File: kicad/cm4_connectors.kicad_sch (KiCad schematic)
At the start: 4 parts, among them U12 2541WV-2X12P

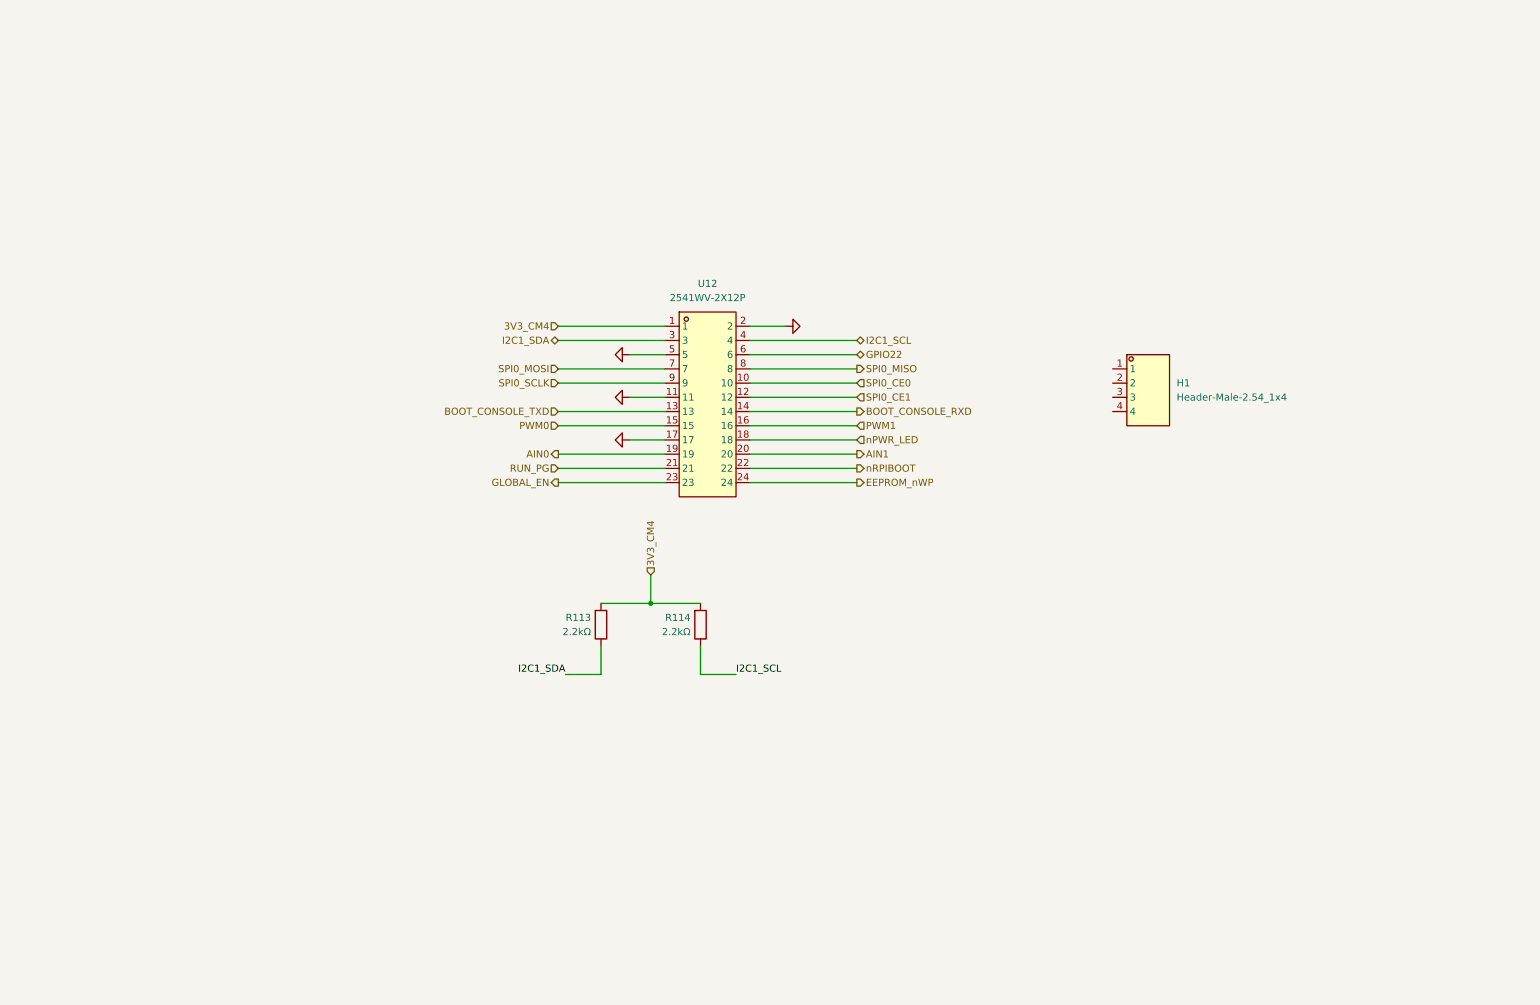
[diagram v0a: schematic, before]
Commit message: GPIO connectors defined
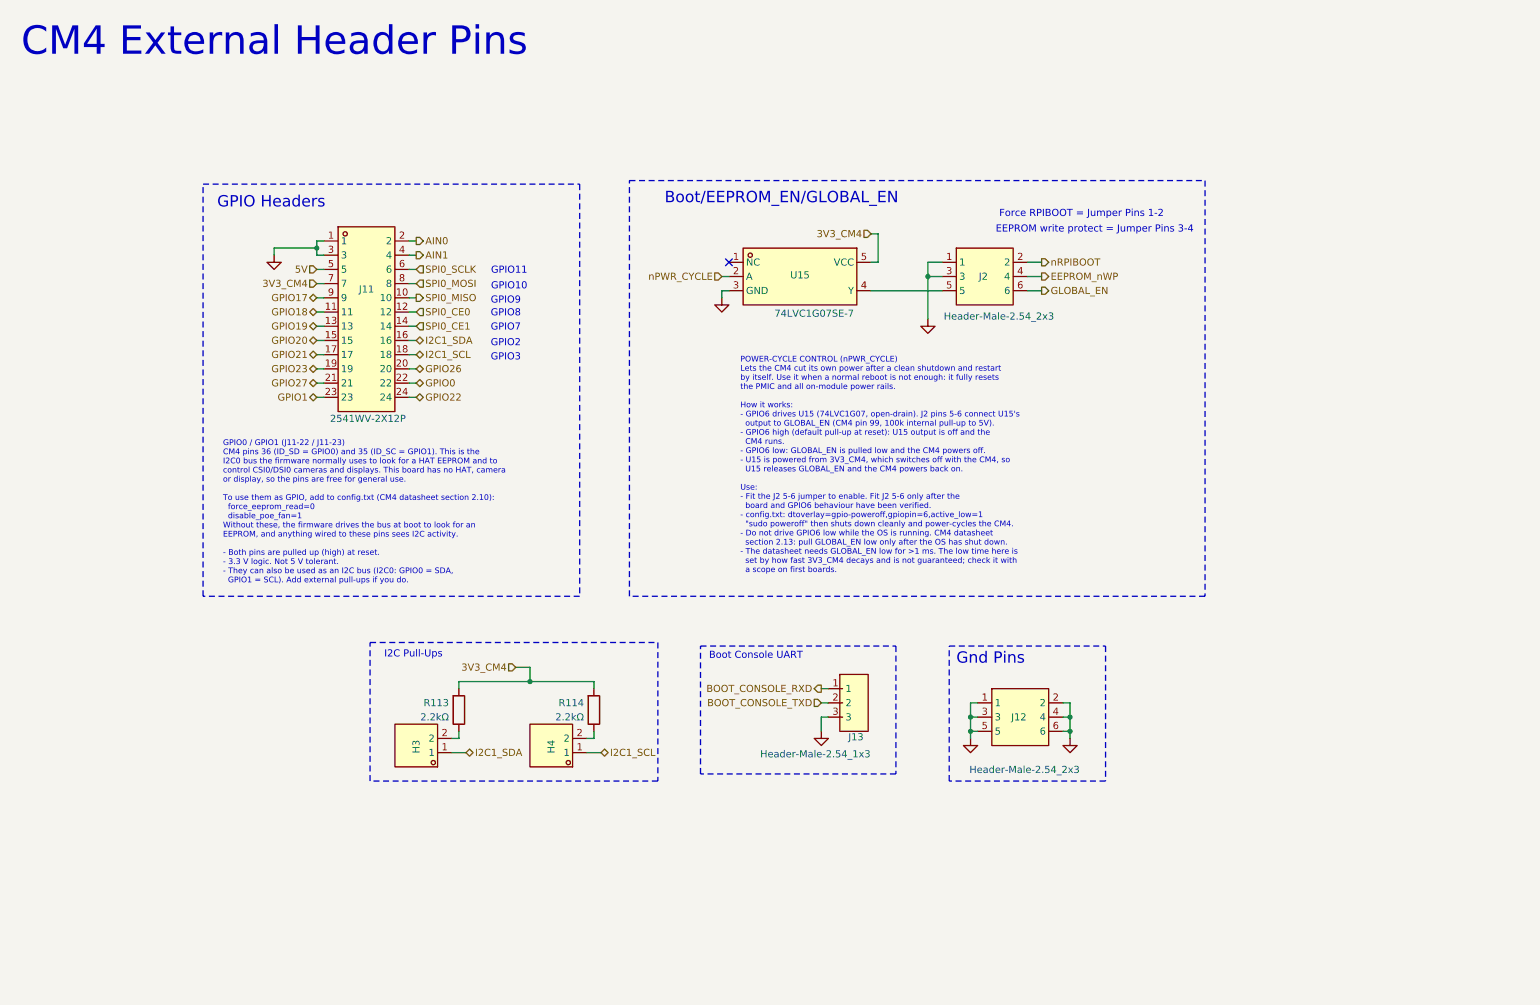
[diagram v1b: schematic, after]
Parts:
- removed H1: Header-Male-2.54_1x4, MyParts:HDR-TH_4P-P2.54-V-M, symbol MyParts:Header-Male-2.54_1x4
- removed U12: 2541WV-2X12P, MyParts:HDR-TH_24P-P2.54-V-M-R2-C12-S2.54, symbol MyParts:2541WV-2X12P
- added H3, H4: 210S-1*2P L=11.6MMGold-plated black, MyParts:HDR-TH_2P-P2.54-V-M-1, symbol MyParts:210S-1*2PL=11.6MMGold-platedblack
- added J11: 2541WV-2X12P, MyParts:HDR-TH_24P-P2.54-V-M-R2-C12-S2.54, symbol MyParts:2541WV-2X12P
- added J12, J2: Header-Male-2.54_2x3, MyParts:HDR-TH_6P-P2.54-V-M-R2-C3-S2.54-1, symbol MyParts:Header-Male-2.54_2x3
- added J13: Header-Male-2.54_1x3, MyParts:HDR-TH_3P-P2.54-V-M-1, symbol MyParts:Header-Male-2.54_1x3
- added U15: 74LVC1G07SE-7, MyParts:SC-88A_L2.0-W1.3-P0.65-LS2.1-BL, symbol MyParts:74LVC1G07SE-7
- R113, R114: footprint PCM_JLCPCB:R_0402 -> MyParts:R0402; symbol PCM_JLCPCB-Resistors:0402,2.2kΩ -> MyParts:0402WGF2201TCE; Attrition Qty 10 -> (none); Category Resistors,Chip Resistor - Surface Mount -> (none); Class Basic Component -> (none); LCSC C25879 -> (none); LCSC Part (none) -> C25879; MPN (none) -> 0402WGF2201TCE; Manufacturer UNI-ROYAL(Uniroyal Elec) -> UNI-ROYAL; Minimum Qty 20 -> (none); Operating Temperature Range -55°C~+155°C -> (none); Overload Voltage (Max) 50V -> (none); Part 0402WGF2201TCE -> (none); Power(Watts) 62.5mW -> (none); Price 0.004USD -> (none); Process SMT -> (none); Resistance 2.2kΩ -> (none); Stock 1767502 -> (none); Temperature Coefficient ±100ppm/°C -> (none); Type Thick Film Resistors -> (none); Voltage Rating (none) -> 50V
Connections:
- net 3V3_CM4: now also J11.7, U15.5 (VCC)
- net AIN0: now also J11.2
- net AIN1: now also J11.4
- net BOOT_CONSOLE_RXD: now also J13.1
- net BOOT_CONSOLE_TXD: now also J13.2
- net EEPROM_nWP: now also J2.4
- net GLOBAL_EN: now also J2.6
- net GND: now also J11.1, J11.3, J12.1, J12.2, J12.3, J12.4, J12.5, J12.6, J13.3, J2.1, J2.3, U15.3 (GND)
- net GPIO22: now also J11.24
- net I2C1_SCL: now also H4.1, J11.18; no longer R114.2
- net I2C1_SDA: now also H3.1, J11.16; no longer R113.2
- net SPI0_CE0: now also J11.12
- net SPI0_CE1: now also J11.14
- net SPI0_MISO: now also J11.10
- net SPI0_MOSI: now also J11.8
- net SPI0_SCLK: now also J11.6
- net nRPIBOOT: now also J2.2
- new net: H3.2, R113.2
- new net: J2.5, U15.4 (Y)
- new net: H4.2, R114.2
- new net 5V: J11.5
- new net GPIO0: J11.22
- new net GPIO1: J11.23
- new net GPIO17: J11.9
- new net GPIO18: J11.11
- new net GPIO19: J11.13
- new net GPIO20: J11.15
- new net GPIO21: J11.17
- new net GPIO23: J11.19
- new net GPIO26: J11.20
- new net GPIO27: J11.21
- new net nPWR_CYCLE: U15.2 (A)
- no-connect marks 0 -> 1
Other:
- note added: "Boot Console UART"
- note added: "Boot/EEPROM_EN/GLOBAL_EN"
- note added: "CM4 External Header Pins"
- note added: "EEPROM write protect = Jumper Pins 3-4"
- note added: "Force RPIBOOT = Jumper Pins 1-2"
- note added: "GPIO Headers"
- note added: "GPIO0 / GPIO1 (J11-22 / J11-23) CM4 pins 36 (ID_SD = GPIO0) and 35 (ID_SC = GPIO1). This is the I2C0 bus the firmware normally uses to look for a HAT EEPROM and to control CSI0/DSI0 cameras and displays. This board has no HAT, camera or display, so the pins are free for general use. To use them as GPIO, add to config.txt (CM4 datasheet section 2.10): force_eeprom_read=0 disable_poe_fan=1 Without 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"
- note added: "GPIO10"
- note added: "GPIO11"
- note added: "GPIO2"
- note added: "GPIO3"
- note added: "GPIO7"
- note added: "GPIO8"
- note added: "GPIO9"
- note added: "Gnd Pins"
- note added: "I2C Pull-Ups"
- note added: "POWER-CYCLE CONTROL (nPWR_CYCLE) Lets the CM4 cut its own power after a clean shutdown and restart by itself. Use it when a normal reboot is not enough: it fully resets the PMIC and all on-module power rails. How it works: - GPIO6 drives U15 (74LVC1G07, open-drain). J2 pins 5-6 connect U15's output to GLOBAL_EN (CM4 pin 99, 100k internal pull-up to 5V). - GPIO6 high (default pull-up at reset): U1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"
- moved on the sheet: R113, R114

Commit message: schematic cleanup
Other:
- note added: "H3, H4: Pull-up resistors for I2C1_SDA/I2C1_SCL. Place jumpers to apply pull-ups."
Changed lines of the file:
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@@
 	(rectangle
 		(start 80.645 130.175)
-		(end 132.08 154.94)
+		(end 132.08 163.83)
 		(stroke
 			(width 0)
@@
 		)
 	)
+	(text "H3, H4:\nPull-up resistors for I2C1_SDA/I2C1_SCL.\nPlace jumpers to apply pull-ups."
+		(exclude_from_sim no)
+		(at 87.376 158.242 0)
+		(effects
+			(font
+				(size 1.27 1.27)
+			)
+			(justify left)
+		)
+	)

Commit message: Still refining
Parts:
- H3, H4: Pkg Type (none) -> THT Pin header 1x2 P2.54
- J11: Pkg Type (none) -> THT Pin header 2x12 P2.54
- J12, J2: Pkg Type (none) -> THT Pin header 2x3 P2.54
- J13: Pkg Type (none) -> THT Pin header 1x3 P2.54
- R113, R114: Pkg Type (none) -> SMD 0402
- U15: Pkg Type (none) -> SMD SOT-353 (SC-88A)
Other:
- note added: "AIN0 / AIN1 (J11-2 / J11-4) to CM4 AnalogIP0/1 (MxL7704 ADC). Measures 0 to 2.55 V (8-bit). Input current < 1 uA (10 Mohm). Survives +6.0 V / -0.3 V DC at the connector (MxL7704 abs max). Not reverse-polarity tolerant. R133/R134 1k series (RCM4 sheet)."
- moved on the sheet: H3, H4, R113, R114

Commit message: Mods
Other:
- note added: "AIN0 / AIN1 (J11-2 / J11-4), field wired, to CM4 AnalogIP0/1 (MxL7704 ADC). Measures 0 to 2.55 V (8-bit). Survives +/-24 V either polarity: R133/R134 10k series + D54/D55 BAT54S clamps to GND and 3V3_CM4 (RCM4 sheet) hold the pins within -0.3 V / +3.6 V (abs max -0.3/+6.0). Error: ADC input < 1 uA x 10k = 10 mV, plus clamp leakage (up to ~1-2 % hot). With the CM4 off, a driven input feeds < 0.3 m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"
- note added: "EEPROM WRITE PROTECT (EEPROM_nWP, J2 3-4) The CM4 pulls EEPROM_nWP up internally (100k), so the bootloader EEPROM is writable unless J2 3-4 is fitted. The jumper only takes effect once protection is enabled in the bootloader config (CM4 datasheet 2.18). Production: - Set eeprom_write_protect=1 in the bootloader config (via usbboot or rpi-eeprom-config) before shipping. - Fit the J2 3-4 jumper. Th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"
- note added: "H3/H4: optional I2C1 pull-ups, normally OPEN. CM4 already pulls GPIO2/3 up with 1.8k (DS p.7). Fit both only for a long, high-capacitance bus at 400 kHz: ~1k total, ~2.9 mA sink at 0.4 V (I2C spec min 3 mA, so compliant devices are OK)."
- note removed: "AIN0 / AIN1 (J11-2 / J11-4) to CM4 AnalogIP0/1 (MxL7704 ADC). Measures 0 to 2.55 V (8-bit). Input current < 1 uA (10 Mohm). Survives +6.0 V / -0.3 V DC at the connector (MxL7704 abs max). Not reverse-polarity tolerant. R133/R134 1k series (RCM4 sheet)."
- note removed: "H3, H4: Pull-up resistors for I2C1_SDA/I2C1_SCL. Place jumpers to apply pull-ups."
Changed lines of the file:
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@@
 	(rectangle
 		(start 127 47.625)
-		(end 229.87 121.92)
+		(end 283.21 121.92)
 		(stroke
 			(width 0)
@@
 		)
 	)
-	(text "H3, H4:\nPull-up resistors for I2C1_SDA/I2C1_SCL.\nPlace jumpers to apply pull-ups."
+	(text "EEPROM WRITE PROTECT (EEPROM_nWP, J2 3-4)\nThe CM4 pulls EEPROM_nWP up internally (100k), so the\nbootloader EEPROM is writable unless J2 3-4 is fitted.\nThe jumper only takes effect once protection is enabled\nin the bootloader config (CM4 datasheet 2.18).\n\nProduction:\n- Set eeprom_write_protect=1 in the bootloader config\n  (via usbboot or rpi-eeprom-config) before shipping.\n- Fit the J2 3-4 jumper. The EEPROM is then protected\n  from power-up (CM4 datasheet 5.1).\n\nBootloader update:\n- Remove J2 3-4, update via usbboot or self-update,\n  then refit the jumper.\n\nWhy not a GPIO with a pull-down: CM4 EEPROM updates run\nonly via usbboot or bootloader self-update (datasheet\n6.3), before Linux can drive a GPIO, so the pin could\nnever be released for an update."
 		(exclude_from_sim no)
-		(at 125.476 187.452 0)
+		(at 231.14 84.455 0)
 		(effects
 			(font
-				(size 1.27 1.27)
+				(size 1.016 1.016)
+			)
+			(justify left)
+		)
+	)
+	(text "H3/H4: optional I2C1 pull-ups, normally OPEN.\nCM4 already pulls GPIO2/3 up with 1.8k (DS p.7).\nFit both only for a long, high-capacitance bus\nat 400 kHz: ~1k total, ~2.9 mA sink at 0.4 V\n(I2C spec min 3 mA, so compliant devices are OK)."
+		(exclude_from_sim no)
+		(at 120.65 187.452 0)
+		(effects
+			(font
+				(size 1.016 1.016)
 			)
 			(justify left)
@@
 		)
 	)
-	(text "AIN0 / AIN1 (J11-2 / J11-4)\nto CM4 AnalogIP0/1 (MxL7704 ADC).\nMeasures 0 to 2.55 V (8-bit).\nInput current < 1 uA (10 Mohm).\nSurvives +6.0 V / -0.3 V DC at\nthe connector (MxL7704 abs max).\nNot reverse-polarity tolerant.\nR133/R134 1k series (RCM4 sheet)."
+	(text "AIN0 / AIN1 (J11-2 / J11-4), field wired, to CM4\nAnalogIP0/1 (MxL7704 ADC). Measures 0 to 2.55 V (8-bit).\nSurvives +/-24 V either polarity: R133/R134 10k series\n+ D54/D55 BAT54S clamps to GND and 3V3_CM4 (RCM4 sheet)\nhold the pins within -0.3 V / +3.6 V (abs max -0.3/+6.0).\nError: ADC input < 1 uA x 10k = 10 mV, plus clamp leakage\n(up to ~1-2 % hot). With the CM4 off, a driven input feeds\n< 0.3 mA (at 6 V) into 3V3_CM4 through the upper clamp."
 		(exclude_from_sim no)
 		(at 55.626 138.176 0)
 		(effects
 			(font
-				(size 1.27 1.27)
+				(size 1.016 1.016)
 			)
 			(justify left bottom)

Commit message: Ready to start layout
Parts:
- renumbered H3 to H5, H4 to H6, J2 to J3, J11 to J4, J13 to J5, J12 to J6, R113 to R20, R114 to R21, U15 to U10
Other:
- note added: "AIN0 / AIN1 (J4-2 / J4-4), field wired, to CM4 AnalogIP0/1 (MxL7704 ADC). Measures 0 to 2.55 V (8-bit). Survives +/-24 V either polarity: R7/R6 10k series + D4/D5 BAT54S clamps to GND and 3V3_CM4 (RCM4 sheet) hold the pins within -0.3 V / +3.6 V (abs max -0.3/+6.0). Error: ADC input < 1 uA x 10k = 10 mV, plus clamp leakage (up to ~1-2 % hot). With the CM4 off, a driven input feeds < 0.3 mA (at 6 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"
- note added: "EEPROM WRITE PROTECT (EEPROM_nWP, J3 3-4) The CM4 pulls EEPROM_nWP up internally (100k), so the bootloader EEPROM is writable unless J3 3-4 is fitted. The jumper only takes effect once protection is enabled in the bootloader config (CM4 datasheet 2.18). Production: - Set eeprom_write_protect=1 in the bootloader config (via usbboot or rpi-eeprom-config) before shipping. - Fit the J3 3-4 jumper. Th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"
- note added: "GPIO0 / GPIO1 (J4-22 / J4-23) CM4 pins 36 (ID_SD = GPIO0) and 35 (ID_SC = GPIO1). This is the I2C0 bus the firmware normally uses to look for a HAT EEPROM and to control CSI0/DSI0 cameras and displays. This board has no HAT, camera or display, so the pins are free for general use. To use them as GPIO, add to config.txt (CM4 datasheet section 2.10): force_eeprom_read=0 disable_poe_fan=1 Without th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"
- note added: "H5/H6: optional I2C1 pull-ups, normally OPEN. CM4 already pulls GPIO2/3 up with 1.8k (DS p.7). Fit both only for a long, high-capacitance bus at 400 kHz: ~1k total, ~2.9 mA sink at 0.4 V (I2C spec min 3 mA, so compliant devices are OK)."
- note added: "POWER-CYCLE CONTROL (nPWR_CYCLE) Lets the CM4 cut its own power after a clean shutdown and restart by itself. Use it when a normal reboot is not enough: it fully resets the PMIC and all on-module power rails. How it works: - GPIO6 drives U10 (74LVC1G07, open-drain). J3 pins 5-6 connect U10's output to GLOBAL_EN (CM4 pin 99, 100k internal pull-up to 5V). - GPIO6 high (default pull-up at reset): U1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"
- note removed: "AIN0 / AIN1 (J11-2 / J11-4), field wired, to CM4 AnalogIP0/1 (MxL7704 ADC). Measures 0 to 2.55 V (8-bit). Survives +/-24 V either polarity: R133/R134 10k series + D54/D55 BAT54S clamps to GND and 3V3_CM4 (RCM4 sheet) hold the pins within -0.3 V / +3.6 V (abs max -0.3/+6.0). Error: ADC input < 1 uA x 10k = 10 mV, plus clamp leakage (up to ~1-2 % hot). With the CM4 off, a driven input feeds < 0.3 m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"
- note removed: "EEPROM WRITE PROTECT (EEPROM_nWP, J2 3-4) The CM4 pulls EEPROM_nWP up internally (100k), so the bootloader EEPROM is writable unless J2 3-4 is fitted. The jumper only takes effect once protection is enabled in the bootloader config (CM4 datasheet 2.18). Production: - Set eeprom_write_protect=1 in the bootloader config (via usbboot or rpi-eeprom-config) before shipping. - Fit the J2 3-4 jumper. Th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"
- note removed: "GPIO0 / GPIO1 (J11-22 / J11-23) CM4 pins 36 (ID_SD = GPIO0) and 35 (ID_SC = GPIO1). This is the I2C0 bus the firmware normally uses to look for a HAT EEPROM and to control CSI0/DSI0 cameras and displays. This board has no HAT, camera or display, so the pins are free for general use. To use them as GPIO, add to config.txt (CM4 datasheet section 2.10): force_eeprom_read=0 disable_poe_fan=1 Without 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"
- note removed: "H3/H4: optional I2C1 pull-ups, normally OPEN. CM4 already pulls GPIO2/3 up with 1.8k (DS p.7). Fit both only for a long, high-capacitance bus at 400 kHz: ~1k total, ~2.9 mA sink at 0.4 V (I2C spec min 3 mA, so compliant devices are OK)."
- note removed: "POWER-CYCLE CONTROL (nPWR_CYCLE) Lets the CM4 cut its own power after a clean shutdown and restart by itself. Use it when a normal reboot is not enough: it fully resets the PMIC and all on-module power rails. How it works: - GPIO6 drives U15 (74LVC1G07, open-drain). J2 pins 5-6 connect U15's output to GLOBAL_EN (CM4 pin 99, 100k internal pull-up to 5V). - GPIO6 high (default pull-up at reset): U1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"

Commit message: Improved README
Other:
- note added: "BOOT CONSOLE UART (J5): CM4 UART0, 3.3 V logic, 115200 baud, 8N1, no flow control J5-1 BOOT_CONSOLE_RXD (GPIO15, CM4 receives) <- adapter TXD J5-2 BOOT_CONSOLE_TXD (GPIO14, CM4 transmits) -> adapter RXD J5-3 GND -- adapter GND TX and RX cross over: the adapter TXD goes to the CM4 RXD. Use an inexpensive USB-to-TTL serial cable (PL2303 / CP2102 / FTDI type) with female jumper leads. Typical colour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"
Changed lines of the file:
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@@
+		)
+	)
+	(text "BOOT CONSOLE UART (J5): CM4 UART0, 3.3 V logic, 115200 baud, 8N1, no flow control\n  J5-1  BOOT_CONSOLE_RXD (GPIO15, CM4 receives)   <- adapter TXD\n  J5-2  BOOT_CONSOLE_TXD (GPIO14, CM4 transmits)  -> adapter RXD\n  J5-3  GND                                       -- adapter GND\nTX and RX cross over: the adapter TXD goes to the CM4 RXD.\n\nUse an inexpensive USB-to-TTL serial cable (PL2303 / CP2102 / FTDI type) with\nfemale jumper leads. Typical colours: black GND, white RXD, green TXD, red 5V.\nCheck the labels on your cable.\n\nDO NOT connect the adapter 5V lead. The board powers itself and J5 has no 5V pin.\nA loose 5V lead can short to the header or the board, so it is best to cut it off\n(or insulate it).\nUse an adapter with 3.3 V signals only. CM4 GPIOs are not 5 V tolerant: check that\nthe adapter TXD idles at about 3.3 V with a meter before connecting.\n\nLinux console: enable_uart=1 in config.txt (Pi OS cmdline.txt already has\nconsole=serial0,115200).\nBootloader messages: set BOOT_UART=1 in the EEPROM config (rpi-eeprom-config)."
+		(exclude_from_sim no)
+		(at 16.51 147.32 0)
+		(effects
+			(font
+				(size 1.27 1.27)
+			)
+			(justify left top)
 		)
 	)
